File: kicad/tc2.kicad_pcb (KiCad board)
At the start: 2 copper layers, 142.5 x 110 mm, 70 parts, among them Q1 BC546, Q2 BC546, Q3 BC546, Q4 BC546, SW1 SPST, SW2 SPST, U1 USBSERIAL3V3, U2 ESP01, U3 L4978, U4 74LS125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

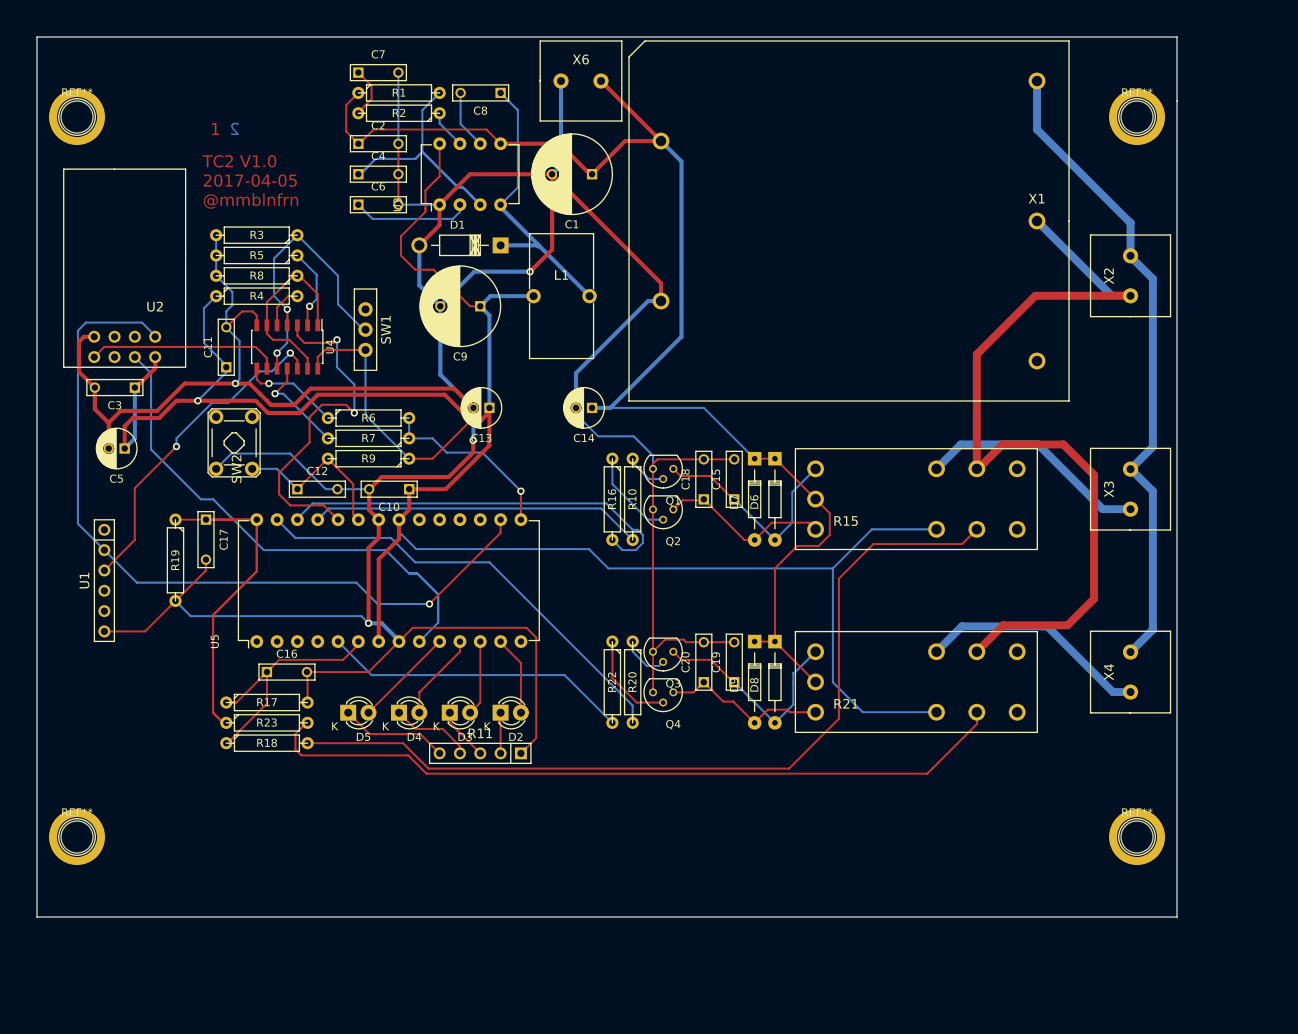
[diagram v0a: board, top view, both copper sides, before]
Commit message: Added some dimension drawing.
Version tagged as 1.1
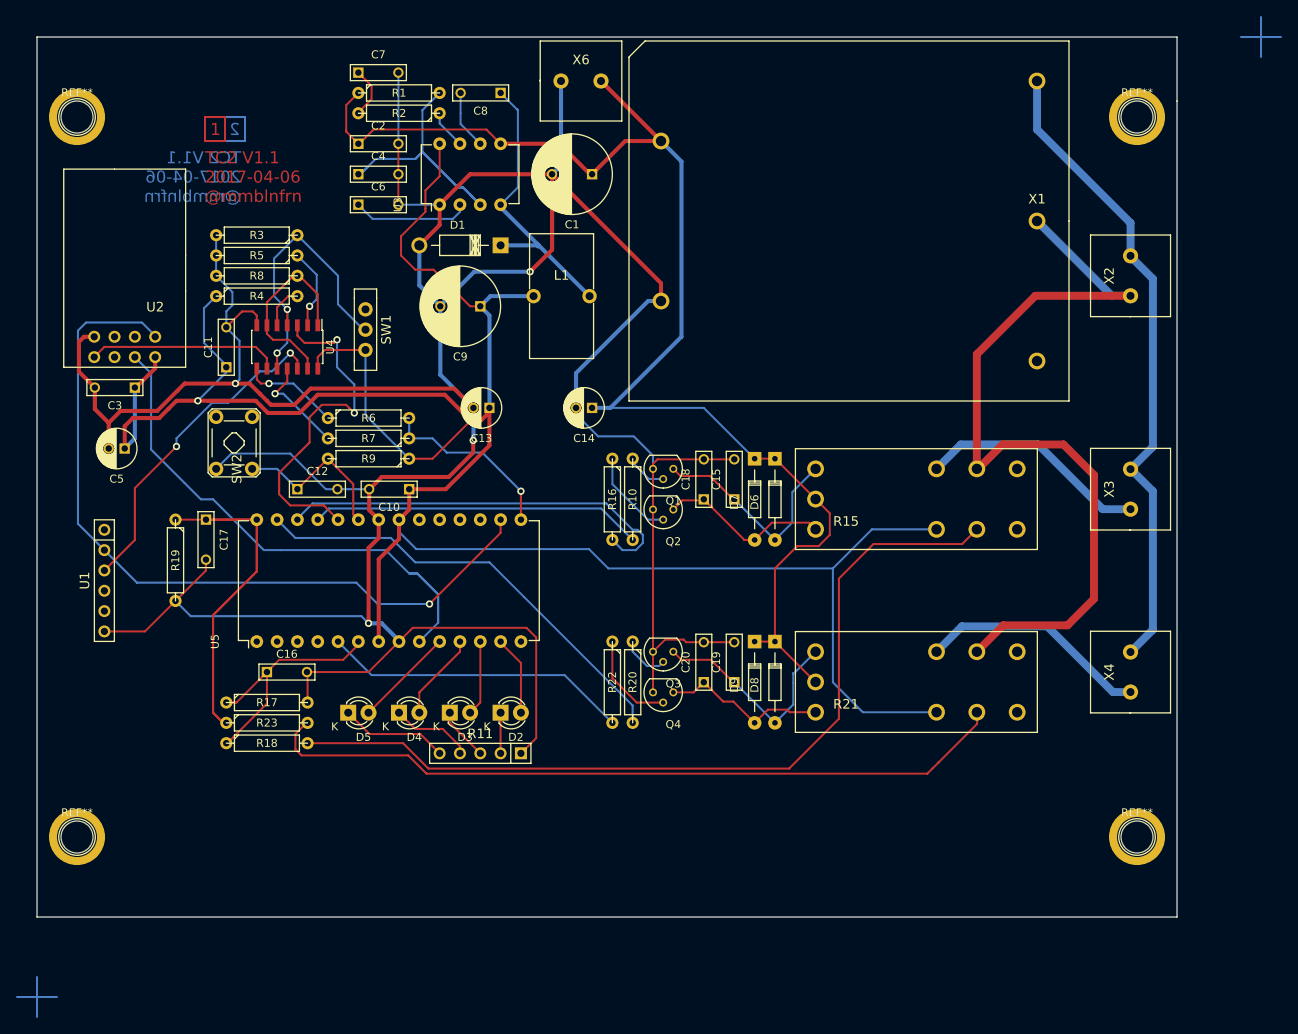
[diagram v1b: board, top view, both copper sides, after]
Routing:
- net (no net): track 0.00 -> 42.0 mm
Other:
- board text added: "TC2 V1.1 2017-04-06 @mmblnfrn"
- board text removed: "TC2 V1.0 2017-04-05 @mmblnfrn"
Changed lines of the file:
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@@
     (links 140)
     (no_connects 0)
-    (area 49.924999 39.924999 192.575001 150.075001)
+    (area 37.135716 33 205.827002 162.827002)
     (thickness 1.6)
-    (drawings 22)
-    (tracks 595)
+    (drawings 23)
+    (tracks 607)
     (zones 0)
     (modules 70)
@@
     (visible_elements FFFCFFFF)
     (pcbplotparams
-      (layerselection 0x008c0_80000001)
+      (layerselection 0x00800_00000000)
       (usegerberextensions false)
       (excludeedgelayer true)
@@
       (padsonsilk false)
       (subtractmaskfromsilk false)
-      (outputformat 3)
+      (outputformat 1)
       (mirror false)
       (drillshape 0)
@@
     (pad 1 thru_hole circle (at 0 0) (size 7 7) (drill 5) (layers *.Cu *.Mask F.SilkS))
   )
+  (gr_text "TC2 V1.1\n2017-04-06\n@mmblnfrn\n" (at 75.5 57.5) (layer B.Cu)
+    (effects (font (size 1.5 1.5) (thickness 0.3)) (justify left mirror))
+  )
+  (gr_text "TC2 V1.1\n2017-04-06 \n@mmblnfrn" (at 71 57.5) (layer F.Cu)
+    (effects (font (size 1.5 1.5) (thickness 0.3)) (justify left))
+  )
   (target plus (at 203 40) (size 5) (width 0.15) (layer Edge.Cuts))
   (target plus (at 50 160) (size 5) (width 0.15) (layer Edge.Cuts))
   (gr_line (start 50 40) (end 50 150) (angle 90) (layer Edge.Cuts) (width 0.15))
-  (gr_text "TC2 V1.0\n2017-04-05\n@mmblnfrn" (at 70.7 58) (layer F.Cu)
-    (effects (font (size 1.5 1.5) (thickness 0.3)) (justify left))
-  )
   (gr_line (start 76 53) (end 71 53) (angle 90) (layer Eco2.User) (width 0.2))
   (gr_line (start 71 50) (end 76 50) (angle 90) (layer Eco2.User) (width 0.2))
@@
   (gr_line (start 192.5 40) (end 192.5 48) (angle 90) (layer Edge.Cuts) (width 0.15))
   (gr_line (start 50 150) (end 50 40) (angle 90) (layer Eco2.User) (width 0.2))
+  (segment (start 47.5 160) (end 52.5 160) (width 0.254) (layer B.Cu) (net 0))
+  (segment (start 50 157.5) (end 50 162.5) (width 0.254) (layer B.Cu) (net 0))
+  (segment (start 200.5 40) (end 205.5 40) (width 0.254) (layer B.Cu) (net 0))
+  (segment (start 203 37.5) (end 203 42.5) (width 0.254) (layer B.Cu) (net 0))
+  (segment (start 73.5 50) (end 76 50) (width 0.25) (layer B.Cu) (net 0))
+  (segment (start 73.5 53) (end 73.5 50) (width 0.25) (layer B.Cu) (net 0))
+  (segment (start 76 53) (end 73.5 53) (width 0.25) (layer B.Cu) (net 0))
+  (segment (start 76 50) (end 76 53) (width 0.25) (layer B.Cu) (net 0))
+  (segment (start 73.5 53) (end 73.5 50) (width 0.25) (layer F.Cu) (net 0))
+  (segment (start 71 50) (end 73.5 50) (width 0.25) (layer F.Cu) (net 0))
+  (segment (start 71 53) (end 71 50) (width 0.25) (layer F.Cu) (net 0))
+  (segment (start 73.5 53) (end 71 53) (width 0.25) (layer F.Cu) (net 0))
   (segment (start 88.646 48.514) (end 88.646 51.816) (width 0.254) (layer F.Cu) (net 1))
   (segment (start 88.646 51.816) (end 88.646 51.689) (width 0.254) (layer F.Cu) (net 1))
